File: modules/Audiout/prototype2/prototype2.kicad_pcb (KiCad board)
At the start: 6 copper layers, 40.6 x 78.7 mm, 8 parts, among them J1 Conn_01x09, U1 TL072

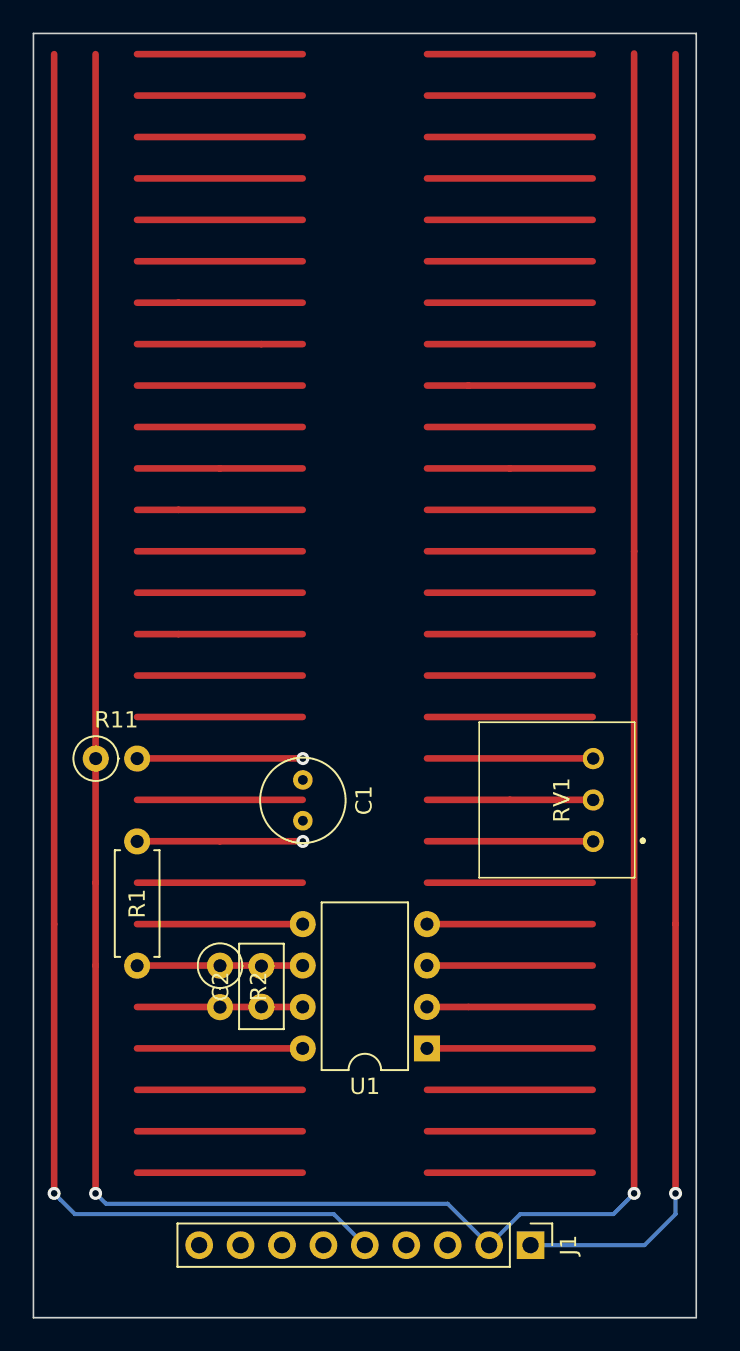
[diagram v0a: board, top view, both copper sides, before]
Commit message: Audiout: Prototype of headphone output - done
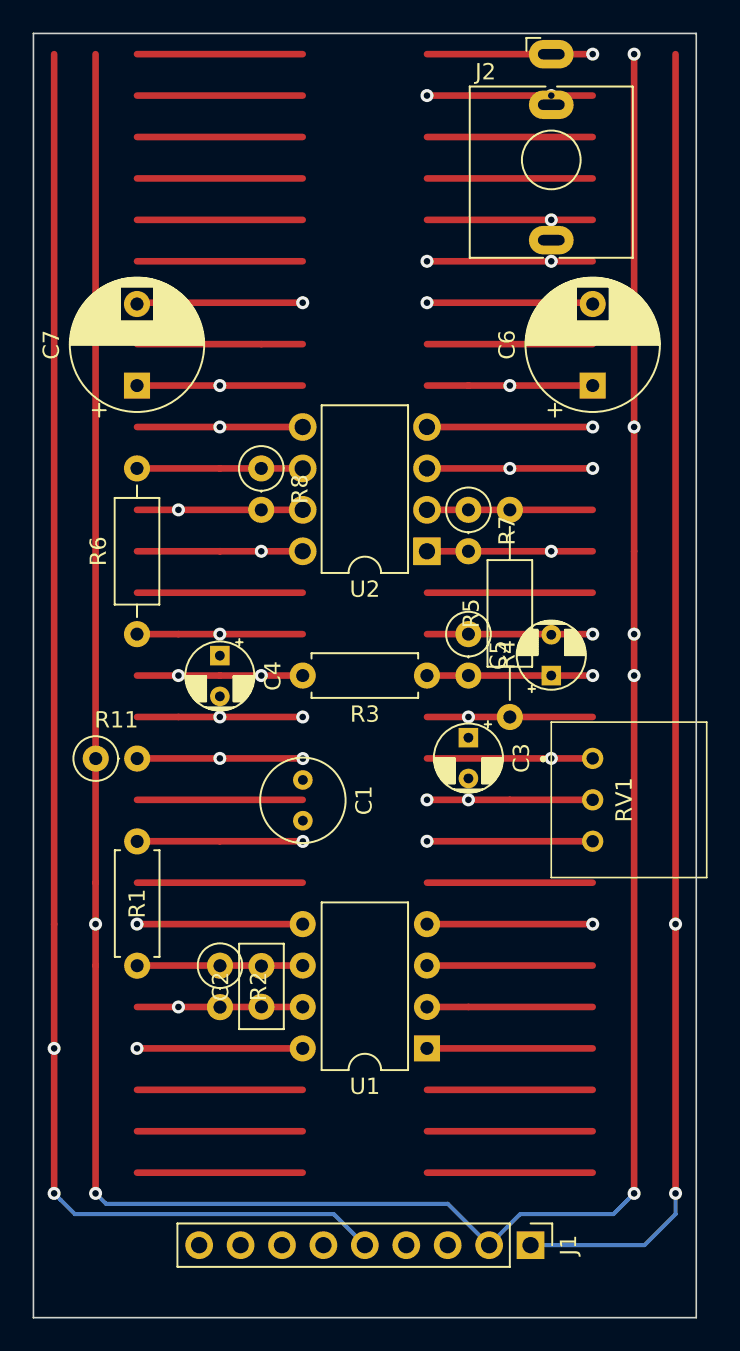
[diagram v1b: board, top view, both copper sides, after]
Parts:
- added C3: 4U7, -lmp-misc:CP_Radial_D4.0mm_P2.50mm, F.Cu at (109.2, 67.3)
- added C4: 4U7, -lmp-misc:CP_Radial_D4.0mm_P2.50mm, F.Cu at (94.0, 62.3)
- added C5: 1U, -lmp-misc:CP_Radial_D4.0mm_P2.50mm, F.Cu at (114.3, 63.5)
- added C6: 220U, Capacitor_THT:CP_Radial_D8.0mm_P5.00mm, F.Cu at (116.8, 45.7)
- added C7: 220U, Capacitor_THT:CP_Radial_D8.0mm_P5.00mm, F.Cu at (88.9, 45.7)
- added J2: WQP419GR, -lmp-synth:Jack_3.5mm_QingPu_WQP-PJ366ST_Vertical, F.Cu at (114.3, 25.4)
- added R3: 100K, -lmp-misc:R_Axial_DIN0207_L6.3mm_D2.5mm_P7.62mm_Horizontal, F.Cu at (106.7, 63.5)
- added R4: 100K, -lmp-stripboard:SB_Gen_1, F.Cu at (109.2, 61.0)
- added R5: 3K9, -lmp-stripboard:SB_Gen_5, F.Cu at (111.8, 66.0)
- added R6: 3K9, -lmp-stripboard:SB_Gen_4, F.Cu at (88.9, 61.0)
- added R7: 3K9, -lmp-stripboard:SB_Gen_1, F.Cu at (109.2, 53.3)
- added R8: 3K9, -lmp-stripboard:SB_Gen_1, F.Cu at (96.5, 50.8)
- added U2: LM4808, -lmp-breakout:Breakout_DIP-8_W7.62mm, F.Cu at (106.7, 55.9)
- moved RV1 3.82 mm to (118.8, 71.1), turned to 90 degrees
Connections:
- RV1 pad 2: unconnected-(RV1-Pad2) -> Net-(C3-Pad2)
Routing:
- net (no net): track 436.9 -> 213.4 mm
- net Net-(C5-Pad1): track 0.00 -> 67.3 mm, vias 0 -> 4
- net +5V: track 0.00 -> 66.1 mm, vias 0 -> 3
- net GND: track 195.7 -> 243.5 mm, vias 2 -> 12
- net Net-(C7-Pad2): track 0.00 -> 36.2 mm, vias 0 -> 3
- net Net-(C6-Pad2): track 0.00 -> 35.6 mm, vias 0 -> 4
- net IN-OUT-1: track 11.5 -> 46.7 mm, vias 1 -> 2
- net Net-(C3-Pad2): track 0.00 -> 32.3 mm, vias 0 -> 4
- net Net-(C6-Pad1): track 0.00 -> 31.1 mm, vias 0 -> 2
- net Net-(C7-Pad1): track 0.00 -> 28.6 mm, vias 0 -> 2
- net Net-(C2-Pad1): track 20.3 -> 40.5 mm, vias 0 -> 2
- net Net-(C4-Pad1): track 0.00 -> 11.5 mm, vias 0 -> 1
- net Net-(C3-Pad1): track 0.00 -> 11.4 mm, vias 0 -> 1
- net unconnected-(RV1-Pad2): track 10.2 -> 0.00 mm
- net Net-(R6-Pad2): track 0.00 -> 10.2 mm
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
